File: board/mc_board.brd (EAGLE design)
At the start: 43.1 x 25 mm, 16 parts, among them IC1 MEGA8-P, Q1 16MHz

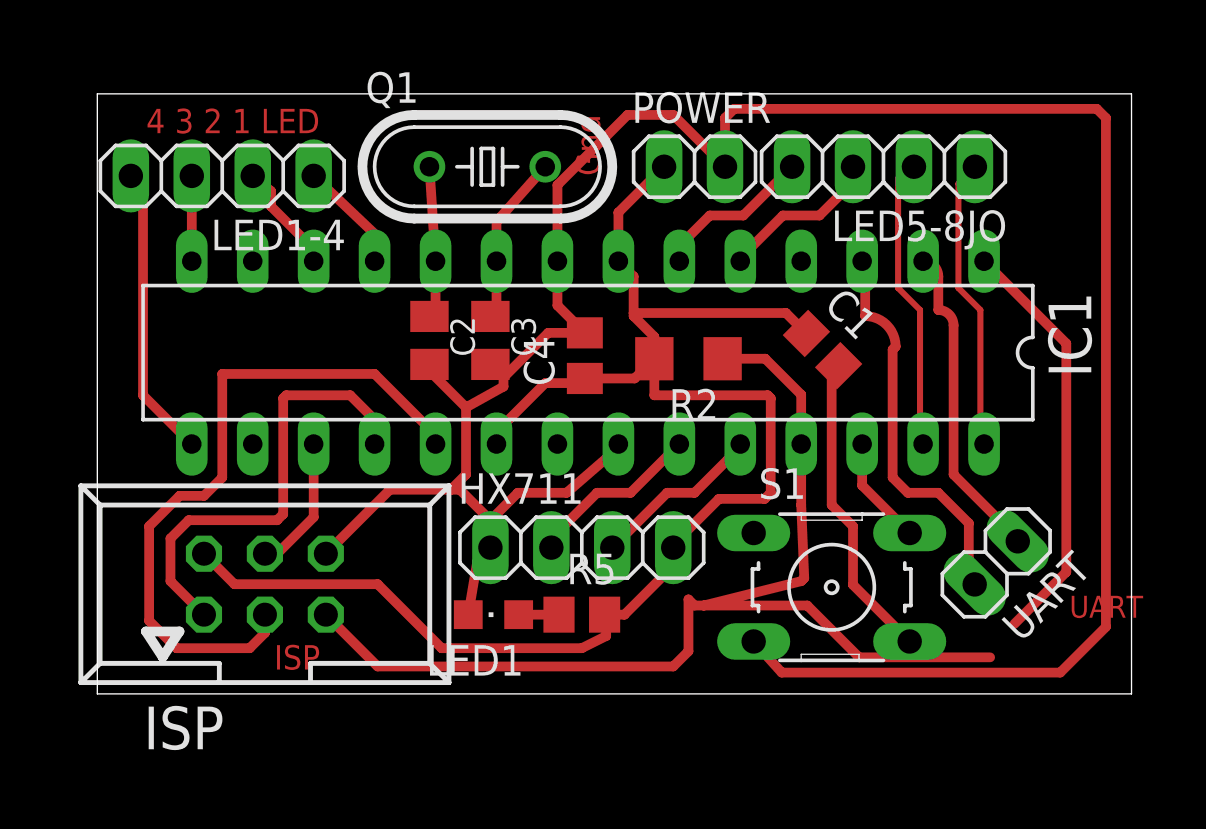
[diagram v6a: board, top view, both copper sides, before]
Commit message: started to swap layer to bottom. not done!
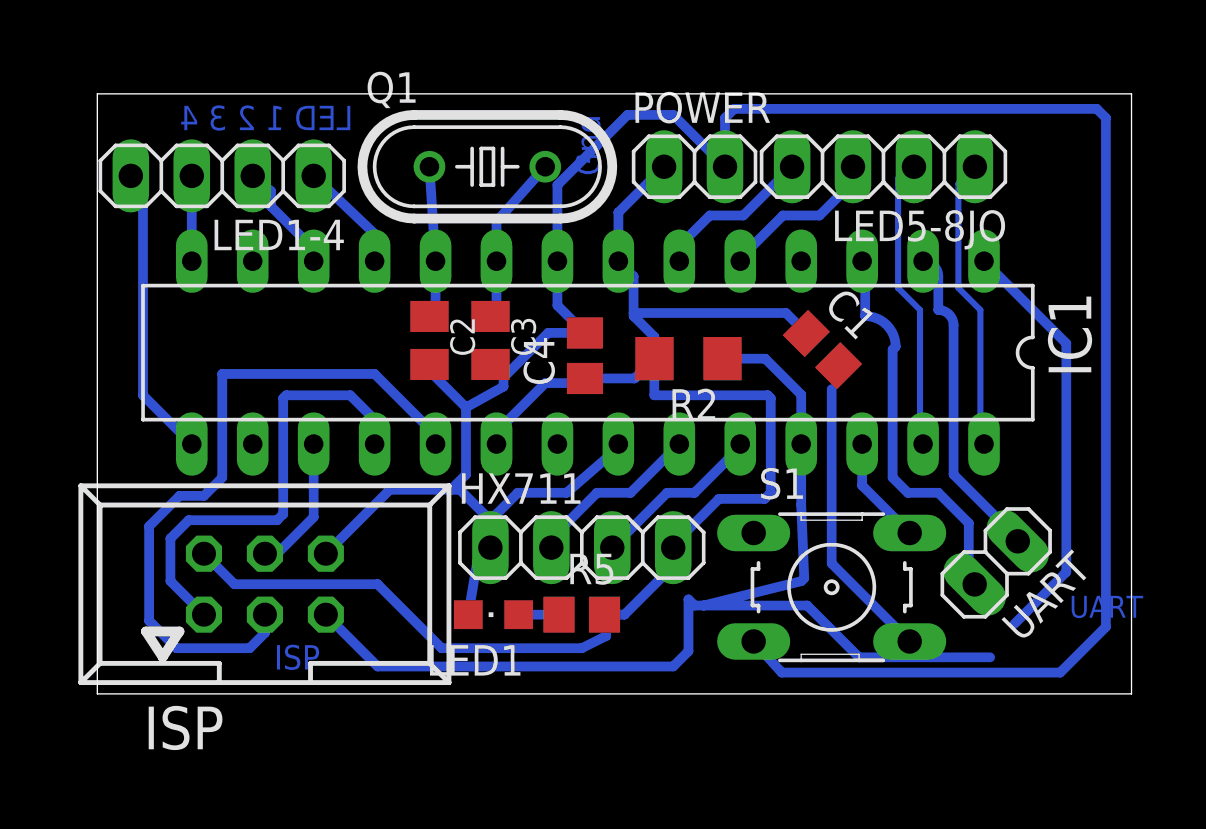
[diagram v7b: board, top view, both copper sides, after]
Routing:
- net N$9: track 13.6 -> 11.9 mm
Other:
- board text added: "LED 1 2 3 4"
- board text removed: "4 3 2 1 LED"
